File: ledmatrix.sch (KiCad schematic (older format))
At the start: 70 parts, among them U2 sled1735

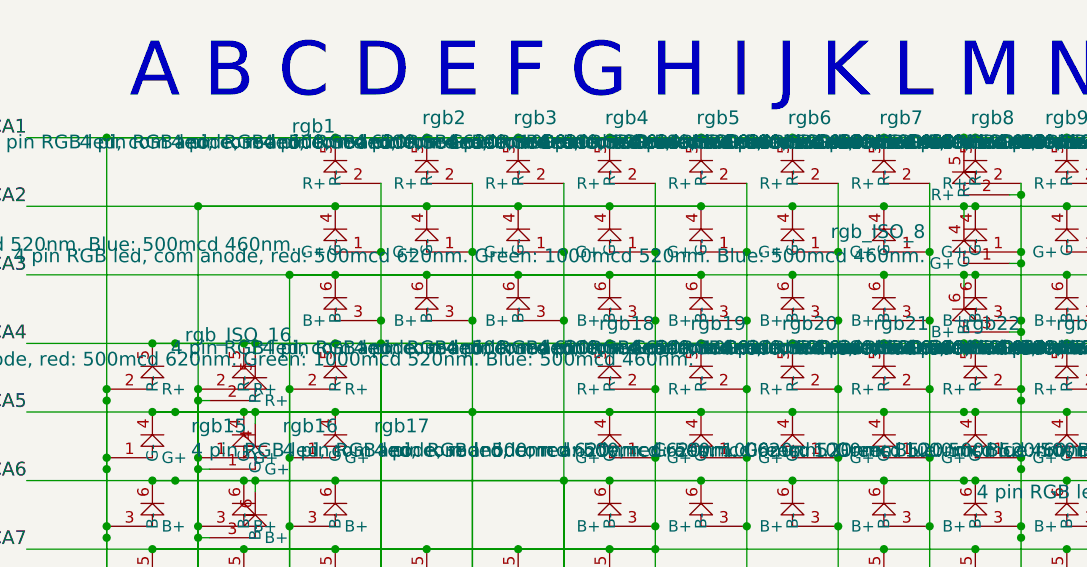
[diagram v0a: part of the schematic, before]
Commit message: fixed diodes
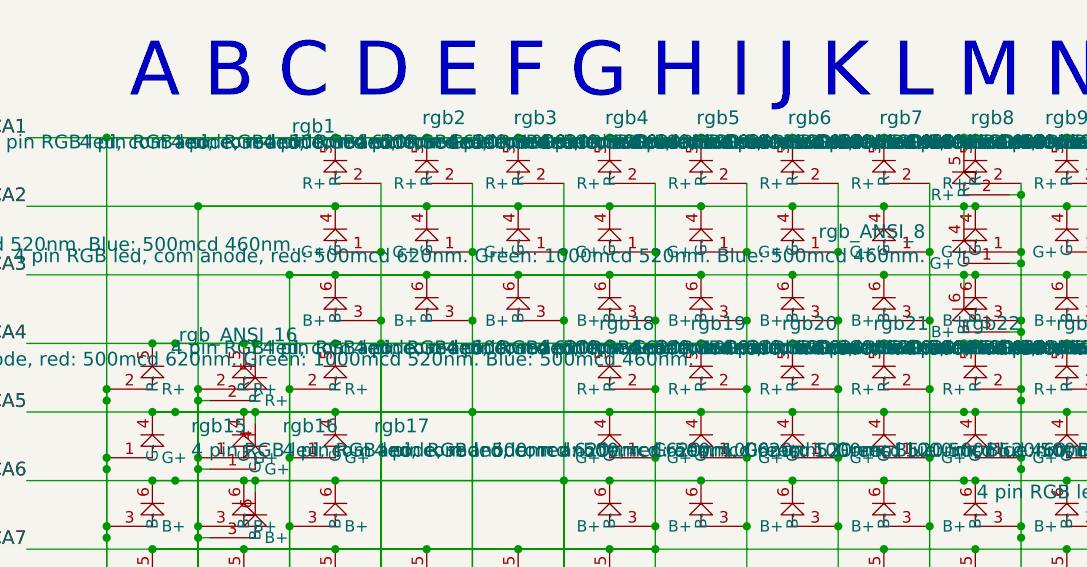
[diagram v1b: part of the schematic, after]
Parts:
- renumbered rgb_ISO_16 to rgb_ANSI_16, rgb_ISO_8 to rgb_ANSI_8
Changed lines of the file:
@@
 $EndComp
 $Comp
-L rgbled rgb_ISO_8
+L rgbled rgb_ANSI_8
 U 1 1 5AE302CF
 P 5100 1550
-F 0 "rgb_ISO_8" H 4931 1689 60  0000 R CNN
+F 0 "rgb_ANSI_8" H 4931 1689 60  0000 R CNN
 F 1 "4 pin RGB led, com anode, red: 500mcd 620nm. Green: 1000mcd 520nm. Blue: 500mcd 460nm." H 4931 1583 60  0000 R CNN
 F 2 "raise_fp:3528-4p-rev" H 5100 1550 60  0001 C CNN
@@
 Connection ~ 1350 2750
 $Comp
-L rgbled rgb_ISO_16
+L rgbled rgb_ANSI_16
 U 1 1 5AE31270
 P 2000 2450
-F 0 "rgb_ISO_16" H 2075 3037 60  0000 C CNN
+F 0 "rgb_ANSI_16" H 2075 3037 60  0000 C CNN
 F 1 "4 pin RGB led, com anode, red: 500mcd 620nm. Green: 1000mcd 520nm. Blue: 500mcd 460nm." H 2075 2931 60  0000 C CNN
 F 2 "raise_fp:3528-4p-rev" H 2000 2450 60  0001 C CNN

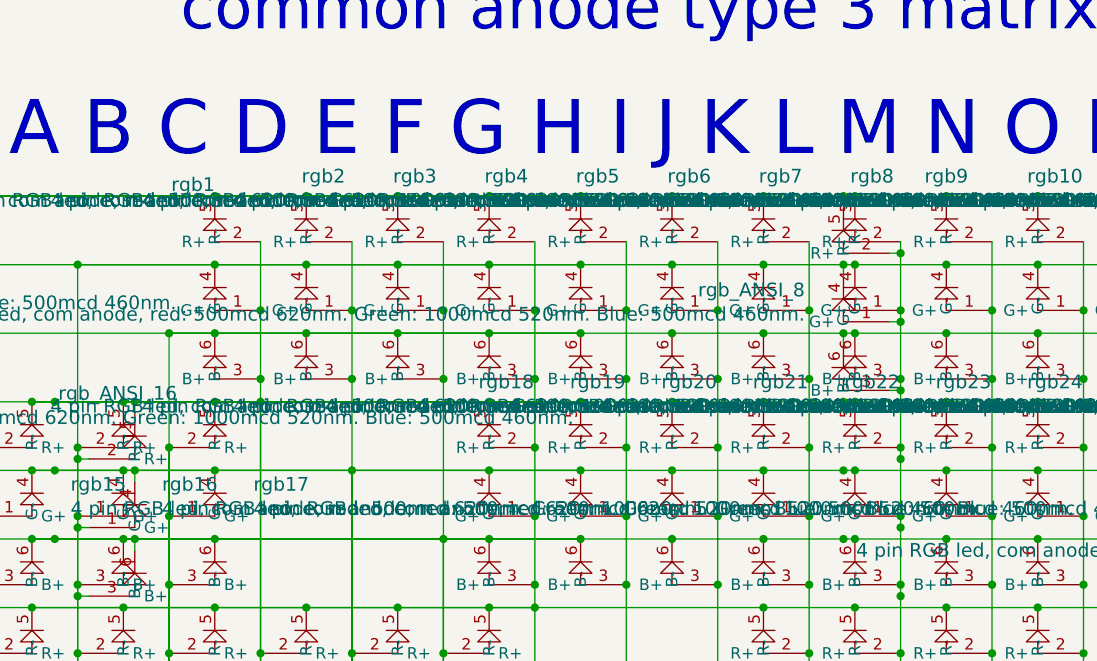
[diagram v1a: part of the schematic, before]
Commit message: iso/ansi component naming
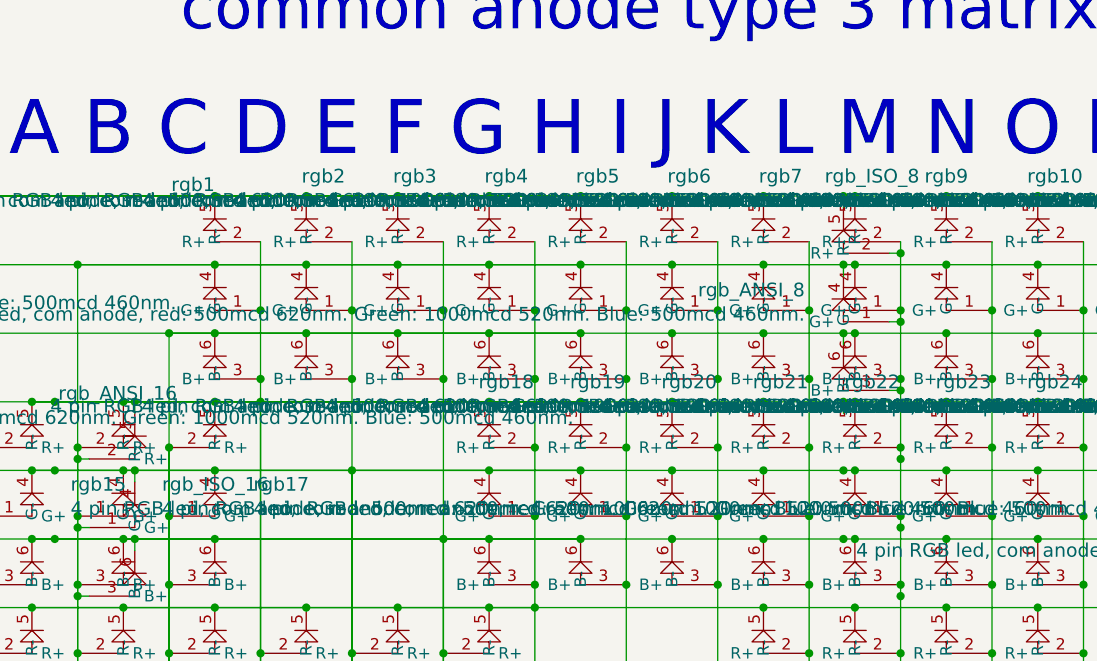
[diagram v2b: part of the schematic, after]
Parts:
- renumbered rgb16 to rgb_ISO_16, rgb8 to rgb_ISO_8
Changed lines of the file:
@@
 $EndComp
 $Comp
-L rgbled rgb8
+L rgbled rgb_ISO_8
 U 1 1 59AEC8B9
 P 5150 1500
-F 0 "rgb8" H 5225 2087 60  0000 C CNN
+F 0 "rgb_ISO_8" H 5225 2087 60  0000 C CNN
 F 1 "4 pin RGB led, com anode, red: 500mcd 620nm. Green: 1000mcd 520nm. Blue: 500mcd 460nm." H 5225 1981 60  0000 C CNN
 F 2 "raise_fp:3528-4p-rev" H 5150 1500 60  0001 C CNN
@@
 $EndComp
 $Comp
-L rgbled rgb16
+L rgbled rgb_ISO_16
 U 1 1 5ADF27D0
 P 1950 2400
-F 0 "rgb16" H 1781 2539 60  0000 R CNN
+F 0 "rgb_ISO_16" H 1781 2539 60  0000 R CNN
 F 1 "4 pin RGB led, com anode, red: 500mcd 620nm. Green: 1000mcd 520nm. Blue: 500mcd 460nm." H 1781 2433 60  0000 R CNN
 F 2 "raise_fp:3528-4p-rev" H 1950 2400 60  0001 C CNN

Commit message: pre autoroute
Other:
- note added: "normal mount\nunderglow"
- note added: "reverse mount \nfor keys"
- note added: "reverse mount\nlow profile"
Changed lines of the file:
@@
 Connection ~ 1350 2450
 Connection ~ 1350 2150
+Wire Notes Line
+	4650 2850 4650 3750
+Wire Notes Line
+	4650 3750 1450 3750
+Wire Notes Line
+	1450 3750 1450 5350
+Wire Notes Line
+	1450 5350 5600 5350
+Wire Notes Line
+	5600 5350 5600 4500
+Wire Notes Line
+	5600 4500 7650 4500
+Wire Notes Line
+	7650 4500 7650 2850
+Wire Notes Line
+	7650 2850 4650 2850
+Text Notes 5100 3950 0    60   ~ 0
+normal mount\nunderglow
+Text Notes 1500 1250 0    60   ~ 0
+reverse mount \nfor keys
+Text Notes 6950 4800 0    60   ~ 0
+reverse mount\nlow profile
 $EndSCHEMATC

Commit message: ansi/iso bom
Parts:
- U2: symbol sled1735-RESCUE-raise-right-asym -> sled1735
- rgb1, rgb10, rgb11, rgb12, rgb13, rgb14, rgb15, rgb17, rgb18, rgb19, rgb2, rgb20, rgb21, rgb22, rgb23, rgb24, rgb25, rgb26, rgb27, rgb28, rgb29, rgb3, rgb30, rgb31, rgb32, rgb33, rgb34, rgb4, rgb5, rgb6, rgb7, rgb9, rgb_ANSI_16, rgb_ANSI_8, rgb_ISO_16, rgb_ISO_8: value 4 pin RGB led, com anode, red: 500mcd 620nm. Green: 1000mcd 520nm. Blue: 500mcd 460nm. -> reverse 4 pin RGB led, com anode
- rgb35, rgb36, rgb37, rgb38, rgb39, rgb40, rgb41, rgb42, rgb43, rgb44, rgb45, rgb46, rgb47, rgb48, rgb49, rgb50, rgb51, rgb52, rgb53, rgb54, rgb55, rgb56, rgb57, rgb58, rgb59, rgb60, rgb61, rgb62, rgb63, rgb64, rgb65, rgb66: value 4 pin RGB led, com anode, red: 500mcd 620nm. Green: 1000mcd 520nm. Blue: 500mcd 460nm. -> 4 pin RGB led, com anode

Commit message: fix qfn56->46 fp name
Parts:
- U2: footprint raise_fp:QFN-56_EP_4.5x6.5_Pitch0.4mm -> raise_fp:QFN-46_EP_4.5x6.5_Pitch0.4mm
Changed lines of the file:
@@
 F 0 "U2" H 10050 2987 60  0000 C CNN
 F 1 "sled1735" H 10050 2881 60  0000 C CNN
-F 2 "raise_fp:QFN-56_EP_4.5x6.5_Pitch0.4mm" H 9850 2250 60  0001 C CNN
+F 2 "raise_fp:QFN-46_EP_4.5x6.5_Pitch0.4mm" H 9850 2250 60  0001 C CNN
 F 3 "" H 9850 2250 60  0001 C CNN
 F 4 "sonix" H 0   0   60  0001 C CNN "supplier"

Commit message: fixes for gp
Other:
- note removed: "RAISE v3\nDYGMA"
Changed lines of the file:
@@
 encoding utf-8
 Sheet 2 2
-Title ""
-Date ""
-Rev ""
-Comp ""
-Comment1 ""
+Title "Raise Right Asym"
+Date "2018-07-09"
+Rev "4.5"
+Comp "Dygma"
+Comment1 "Matt Venn"
 Comment2 ""
 Comment3 ""
@@
 Text Notes 8200 5450 2    197  ~ 0
 1\n2\n3\n4\n5\n6\n7\n8\n9\n10\n11\n12\n13\n14\n15
-Text Notes 7100 7050 0    157  ~ 0
-RAISE v3\nDYGMA
 Wire Wire Line
 	1000 1000 7550 1000

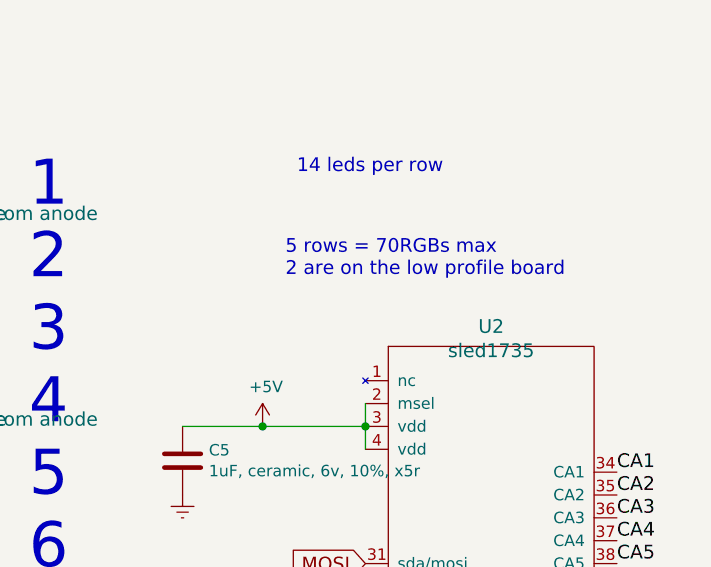
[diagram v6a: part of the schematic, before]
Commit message: changed 47uf ceramic to tantalum
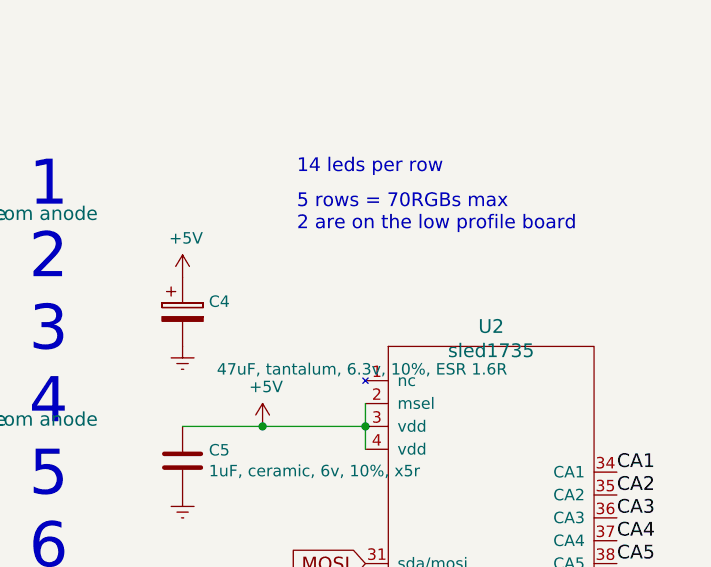
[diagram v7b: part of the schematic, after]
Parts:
- added C4: 47uF, tantalum, 6.3v, 10%, ESR 1.6R, Capacitor_Tantalum_SMD:CP_EIA-3216-18_Kemet-A, symbol CP
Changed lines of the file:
@@
 LIBS:test-jig
 LIBS:usb_c_16pin
+LIBS:Device
 EELAYER 26 0
 EELAYER END
@@
 Text Notes 9200 850  0    60   ~ 0
 14 leds per row
-Text Notes 9150 1300 0    60   ~ 0
+Text Notes 9200 1100 0    60   ~ 0
 5 rows = 70RGBs max\n2 are on the low profile board
 $Comp
@@
 Text Notes 6950 4800 0    60   ~ 0
 reverse mount\nlow profile
+$Comp
+L Earth #PWR022
+U 1 1 5B901616
+P 8700 1600
+F 0 "#PWR022" H 8700 1350 50  0001 C CNN
+F 1 "Earth" H 8700 1450 50  0001 C CNN
+F 2 "" H 8700 1600 50  0000 C CNN
+F 3 "" H 8700 1600 50  0000 C CNN
+	1    8700 1600
+	1    0    0    -1
+$EndComp
+$Comp
+L CP C4
+U 1 1 5B901621
+P 8700 1450
+F 0 "C4" H 8815 1496 50  0000 L CNN
+F 1 "47uF, tantalum, 6.3v, 10%, ESR 1.6R" H 8850 1200 50  0000 L CNN
+F 2 "Capacitor_Tantalum_SMD:CP_EIA-3216-18_Kemet-A" H 8738 1300 50  0001 C CNN
+F 3 "" H 8700 1450 50  0000 C CNN
+F 4 "2333037RL" H 8700 1450 60  0001 C CNN "farnell #"
+F 5 "AVX" H 5900 -5350 60  0001 C CNN "supplier"
+F 6 "TAJA476K006RNJ" H 8700 1450 60  0001 C CNN "supplier PN"
+F 7 "Value" H 8700 1450 60  0001 C CNN "MOQ"
+F 8 "Value" H 8700 1450 60  0001 C CNN "leadtime"
+	1    8700 1450
+	1    0    0    -1
+$EndComp
+$Comp
+L +5V #PWR037
+U 1 1 5B901B79
+P 8700 1300
+F 0 "#PWR037" H 8700 1150 50  0001 C CNN
+F 1 "+5V" H 8715 1473 50  0000 C CNN
+F 2 "" H 8700 1300 50  0000 C CNN
+F 3 "" H 8700 1300 50  0000 C CNN
+	1    8700 1300
+	1    0    0    -1
+$EndComp
 $EndSCHEMATC

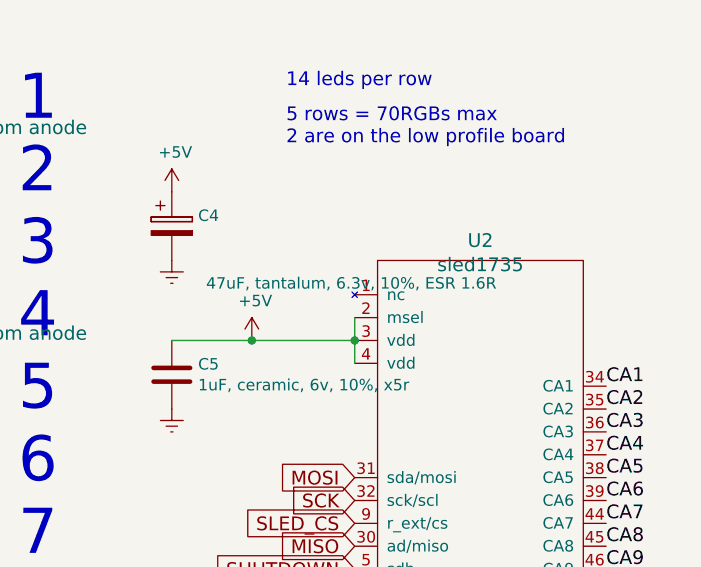
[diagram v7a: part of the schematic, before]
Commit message: derated tantalum to 10v
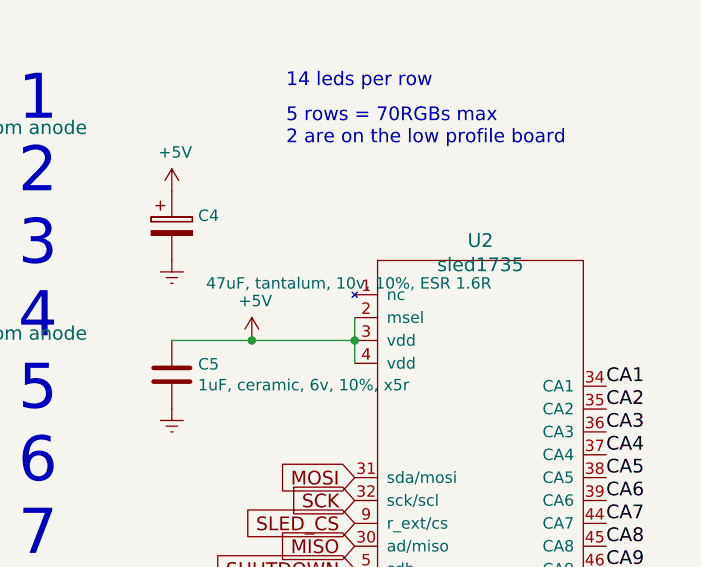
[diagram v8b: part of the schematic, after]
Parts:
- C4: value 47uF, tantalum, 6.3v, 10%, ESR 1.6R -> 47uF, tantalum, 10v, 10%, ESR 1.6R; footprint Capacitor_Tantalum_SMD:CP_EIA-3216-18_Kemet-A -> Capacitor_Tantalum_SMD:CP_EIA-3528-21_Kemet-B; farnell # 2333037RL -> 1432366; supplier PN TAJA476K006RNJ -> TAJB476K010RNJ
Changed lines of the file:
@@
 P 8700 1450
 F 0 "C4" H 8815 1496 50  0000 L CNN
-F 1 "47uF, tantalum, 6.3v, 10%, ESR 1.6R" H 8850 1200 50  0000 L CNN
-F 2 "Capacitor_Tantalum_SMD:CP_EIA-3216-18_Kemet-A" H 8738 1300 50  0001 C CNN
-F 3 "" H 8700 1450 50  0000 C CNN
-F 4 "2333037RL" H 8700 1450 60  0001 C CNN "farnell #"
+F 1 "47uF, tantalum, 10v, 10%, ESR 1.6R" H 8850 1200 50  0000 L CNN
+F 2 "Capacitor_Tantalum_SMD:CP_EIA-3528-21_Kemet-B" H 8738 1300 50  0001 C CNN
+F 3 "http://www.farnell.com/datasheets/2042914.pdf?_ga=2.48992037.208533312.1536141751-2043240940.1516888894&_gac=1.247656181.1532683767.CjwKCAjwhevaBRApEiwA7aT53zTVIy1Ri4nl7qGoZV30uJtjVZm712YCRH0pjFZDdC8St9fAwf9sMBoCBakQAvD_BwE" H 10450 3500 50  0001 C CNN
+F 4 "1432366" H 8700 1450 60  0001 C CNN "farnell #"
 F 5 "AVX" H 5900 -5350 60  0001 C CNN "supplier"
-F 6 "TAJA476K006RNJ" H 8700 1450 60  0001 C CNN "supplier PN"
+F 6 "TAJB476K010RNJ" H 8700 1450 60  0001 C CNN "supplier PN"
 F 7 "Value" H 8700 1450 60  0001 C CNN "MOQ"
 F 8 "Value" H 8700 1450 60  0001 C CNN "leadtime"
